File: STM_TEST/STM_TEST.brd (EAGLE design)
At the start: 59.9 x 69.6 mm, 53 parts, among them U1 TPS2115APWR, U2 AZ1117EH-3.3TRG1, Y1 ECS-80-S-4X, Y2 ECS-80-S-4X

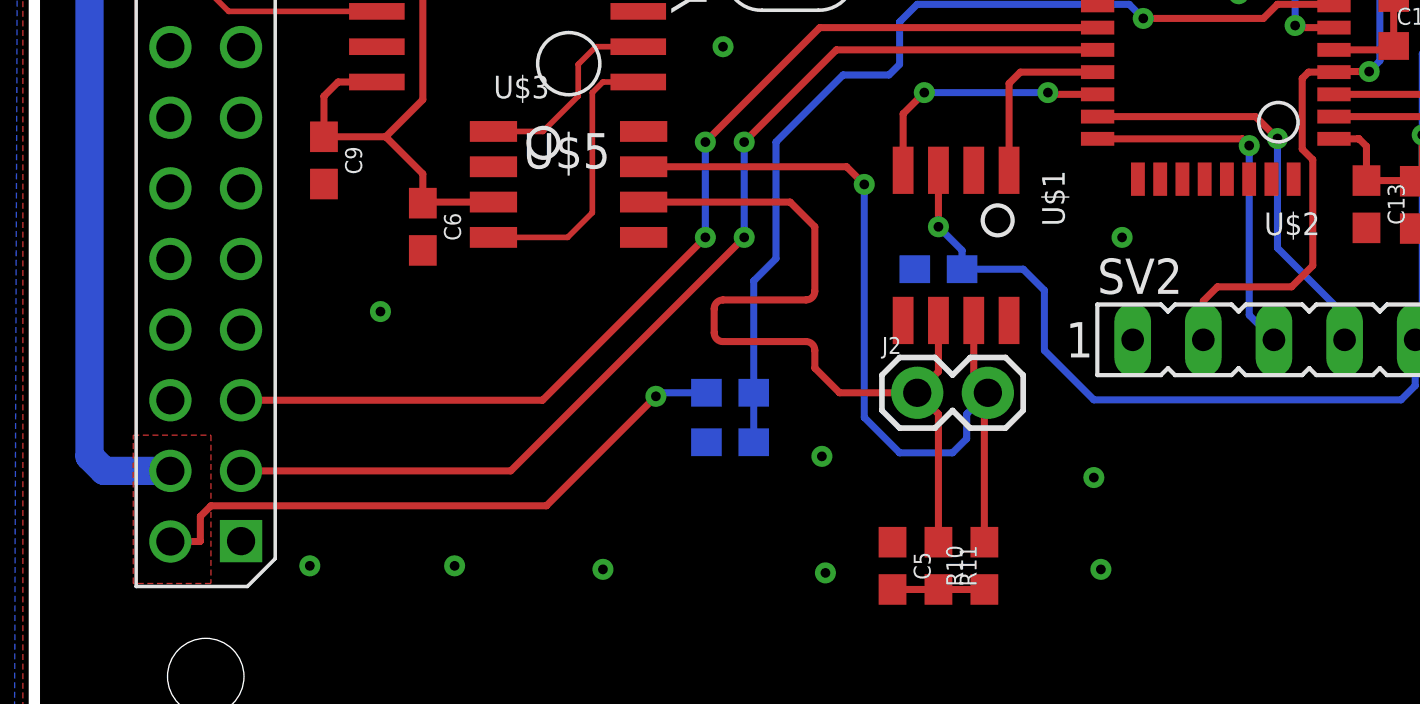
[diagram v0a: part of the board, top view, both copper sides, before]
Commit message: Routed USART
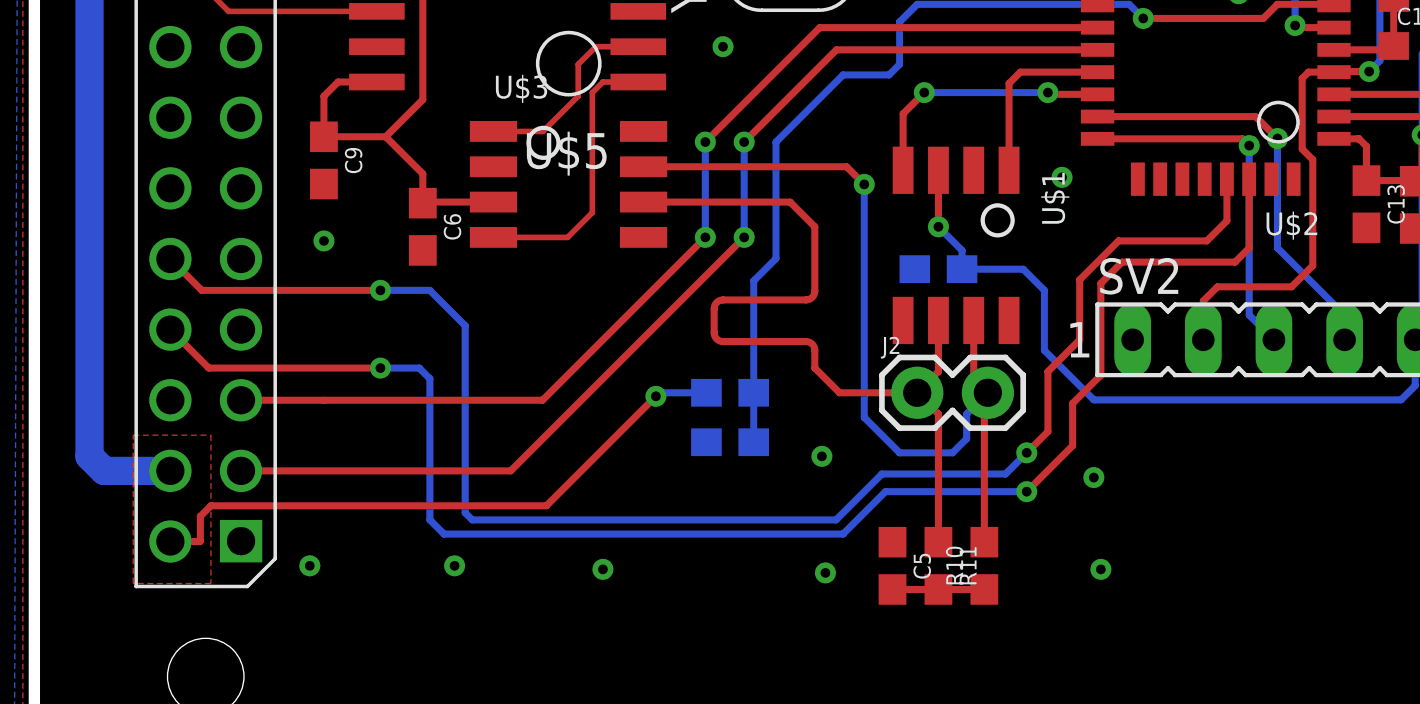
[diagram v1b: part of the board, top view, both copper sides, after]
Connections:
- removed net UART_RXD: PCB1.P$10
- removed net UART_TXD: PCB1.P$8
- new net USART_RX: PCB1.P$8, U$2.PB7
- new net USART_TX: PCB1.P$10, U$2.PB6
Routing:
- net USART_RX: track 0.00 -> 54.4 mm, vias 0 -> 2
- net USART_TX: track 0.00 -> 54.3 mm, vias 0 -> 2
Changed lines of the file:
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@@
 <via x="35.179" y="39.243" extent="1-16" drill="0.35"/>
 <via x="33.782" y="35.306" extent="1-16" drill="0.35"/>
-<via x="12.827" y="17.399" extent="1-16" drill="0.35"/>
+<via x="10.795" y="19.939" extent="1-16" drill="0.35"/>
 <via x="10.287" y="8.255" extent="1-16" drill="0.35"/>
 <via x="15.494" y="8.255" extent="1-16" drill="0.35"/>
@@
 <via x="56.642" y="13.335" extent="1-16" drill="0.35"/>
 <via x="57.023" y="9.398" extent="1-16" drill="0.35"/>
-<via x="39.497" y="20.066" extent="1-16" drill="0.35"/>
+<via x="37.338" y="22.225" extent="1-16" drill="0.35"/>
 <via x="25.146" y="26.924" extent="1-16" drill="0.35"/>
 <via x="40.259" y="59.055" extent="1-16" drill="0.35"/>
@@
 <wire x1="7.366" y1="28.194" x2="12.698" y2="28.194" width="0.2032" layer="1"/>
 </signal>
-<signal name="UART_RXD">
-<contactref element="PCB1" pad="P$10"/>
-</signal>
-<signal name="UART_TXD">
-<contactref element="PCB1" pad="P$8"/>
-</signal>
 <signal name="MISO">
 <contactref element="U$2" pad="PA6"/>
@@
 <contactref element="U$2" pad="PA9"/>
 <contactref element="PCB1" pad="P$5"/>
-<wire x1="7.8122" y1="14.2096" x2="18.6546" y2="14.2096" width="0.254" layer="1"/>
+<wire x1="7.8122" y1="14.2096" x2="10.795" y2="14.2096" width="0.254" layer="1"/>
+<wire x1="10.795" y1="14.2096" x2="18.6546" y2="14.2096" width="0.254" layer="1"/>
 <wire x1="18.6546" y1="14.2096" x2="24.511" y2="20.066" width="0.254" layer="1"/>
 <via x="24.511" y="20.066" extent="1-16" drill="0.35"/>
@@
 <wire x1="21.4" y1="67.608" x2="21.4" y2="65.087" width="1.016" layer="16"/>
 </signal>
+<signal name="USART_RX">
+<contactref element="U$2" pad="PB7"/>
+<contactref element="PCB1" pad="P$8"/>
+<wire x1="5.2722" y1="16.7496" x2="6.6548" y2="15.367" width="0.254" layer="1"/>
+<wire x1="6.6548" y1="15.367" x2="12.827" y2="15.367" width="0.254" layer="1"/>
+<via x="12.827" y="15.367" extent="1-16" drill="0.35"/>
+<wire x1="12.827" y1="15.367" x2="14.224" y2="15.367" width="0.254" layer="16"/>
+<wire x1="14.224" y1="15.367" x2="14.605" y2="14.986" width="0.254" layer="16"/>
+<wire x1="14.605" y1="14.986" x2="14.605" y2="9.906" width="0.254" layer="16"/>
+<wire x1="14.605" y1="9.906" x2="15.113" y2="9.398" width="0.254" layer="16"/>
+<wire x1="15.113" y1="9.398" x2="29.464" y2="9.398" width="0.254" layer="16"/>
+<wire x1="29.464" y1="9.398" x2="30.988" y2="10.922" width="0.254" layer="16"/>
+<via x="36.068" y="10.922" extent="1-16" drill="0.35"/>
+<wire x1="36.068" y1="10.922" x2="37.719" y2="12.573" width="0.254" layer="1"/>
+<wire x1="37.719" y1="12.573" x2="37.719" y2="14.097" width="0.254" layer="1"/>
+<wire x1="37.719" y1="14.097" x2="38.735" y2="15.113" width="0.254" layer="1"/>
+<wire x1="38.735" y1="15.113" x2="38.735" y2="18.415" width="0.254" layer="1"/>
+<wire x1="43.561" y1="19.177" x2="44.069" y2="19.685" width="0.254" layer="1"/>
+<wire x1="44.069" y1="19.685" x2="44.067" y2="19.687" width="0.254" layer="1"/>
+<wire x1="44.067" y1="19.687" x2="44.067" y2="22.16" width="0.254" layer="1"/>
+<wire x1="30.988" y1="10.922" x2="36.068" y2="10.922" width="0.254" layer="16"/>
+<wire x1="38.735" y1="18.415" x2="39.497" y2="19.177" width="0.254" layer="1"/>
+<wire x1="39.497" y1="19.177" x2="43.561" y2="19.177" width="0.254" layer="1"/>
+</signal>
+<signal name="USART_TX">
+<contactref element="U$2" pad="PB6"/>
+<contactref element="PCB1" pad="P$10"/>
+<wire x1="5.2722" y1="19.2896" x2="6.4008" y2="18.161" width="0.254" layer="1"/>
+<wire x1="6.4008" y1="18.161" x2="12.827" y2="18.161" width="0.254" layer="1"/>
+<via x="12.827" y="18.161" extent="1-16" drill="0.35"/>
+<wire x1="12.827" y1="18.161" x2="14.605" y2="18.161" width="0.254" layer="16"/>
+<wire x1="14.605" y1="18.161" x2="15.875" y2="16.891" width="0.254" layer="16"/>
+<wire x1="15.875" y1="16.891" x2="15.875" y2="10.16" width="0.254" layer="16"/>
+<wire x1="15.875" y1="10.16" x2="16.129" y2="9.906" width="0.254" layer="16"/>
+<wire x1="16.129" y1="9.906" x2="29.21" y2="9.906" width="0.254" layer="16"/>
+<wire x1="29.21" y1="9.906" x2="30.861" y2="11.557" width="0.254" layer="16"/>
+<wire x1="35.306" y1="11.557" x2="36.068" y2="12.319" width="0.254" layer="16"/>
+<via x="36.068" y="12.319" extent="1-16" drill="0.35"/>
+<wire x1="36.068" y1="12.319" x2="36.83" y2="13.081" width="0.254" layer="1"/>
+<wire x1="36.83" y1="15.24" x2="37.973" y2="16.383" width="0.254" layer="1"/>
+<wire x1="37.973" y1="18.542" x2="39.37" y2="19.939" width="0.254" layer="1"/>
+<wire x1="39.37" y1="19.939" x2="42.545" y2="19.939" width="0.254" layer="1"/>
+<wire x1="42.545" y1="19.939" x2="43.267" y2="20.661" width="0.254" layer="1"/>
+<wire x1="43.267" y1="20.661" x2="43.267" y2="22.16" width="0.254" layer="1"/>
+<wire x1="30.861" y1="11.557" x2="35.306" y2="11.557" width="0.254" layer="16"/>
+<wire x1="36.83" y1="13.081" x2="36.83" y2="15.24" width="0.254" layer="1"/>
+<wire x1="37.973" y1="16.383" x2="37.973" y2="18.542" width="0.254" layer="1"/>
+</signal>
 </signals>

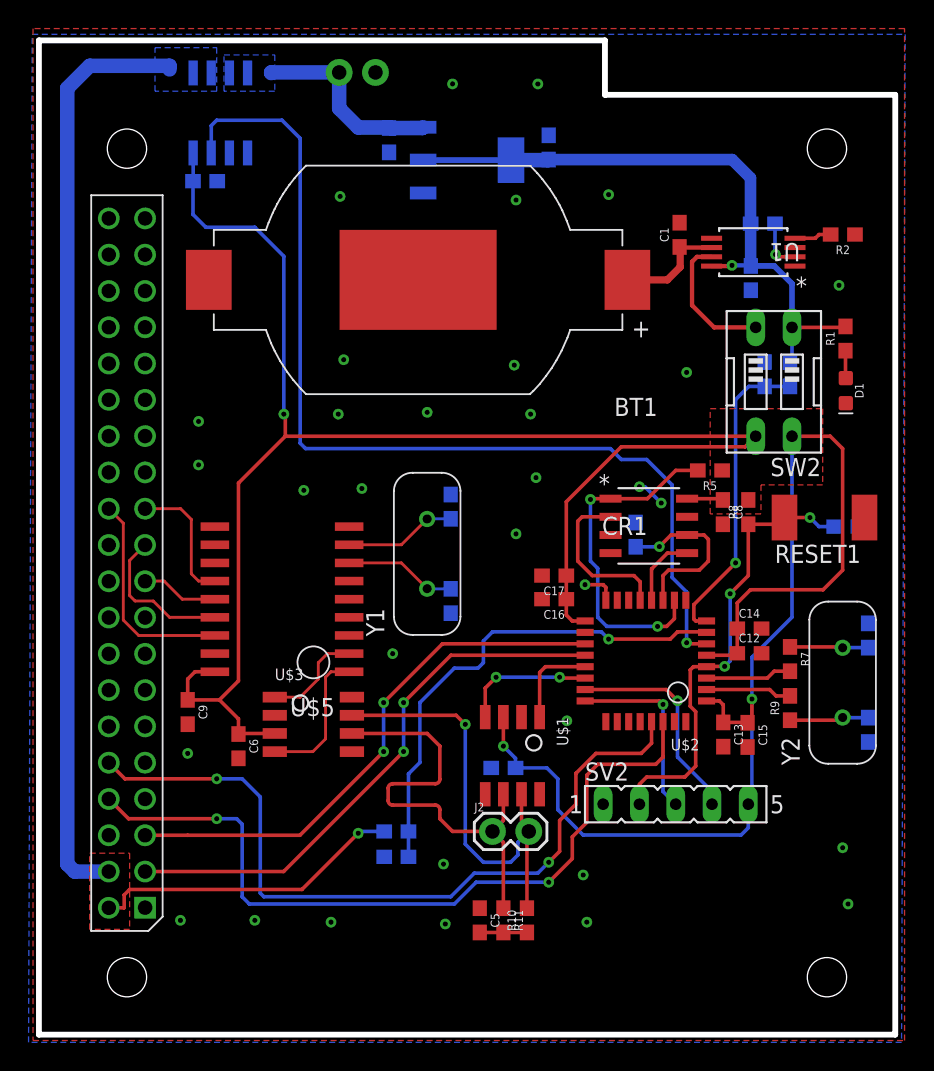
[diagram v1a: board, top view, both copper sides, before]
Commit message: Routing Complete
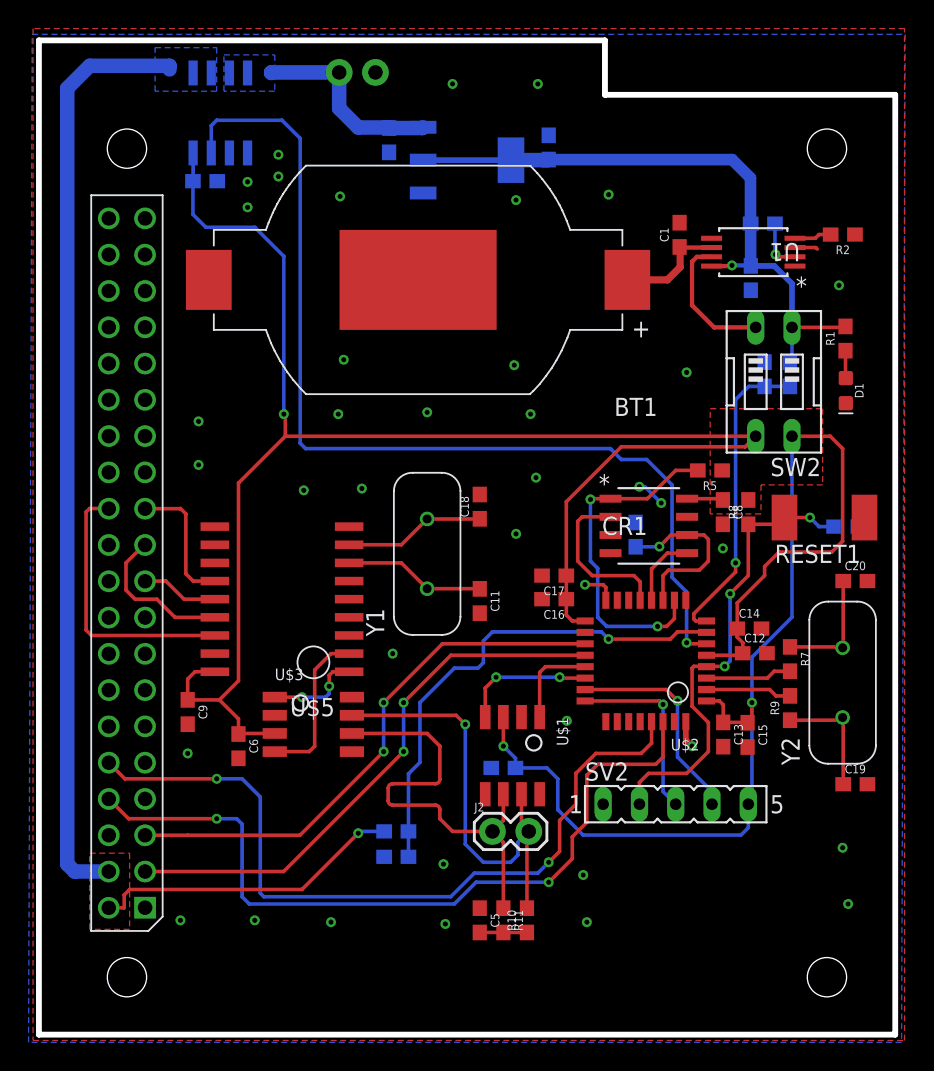
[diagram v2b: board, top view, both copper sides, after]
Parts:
- moved C19 3.91 mm to (57.5, 17.8), flipped to the top, turned to 0 degrees
- moved C20 3.91 mm to (57.5, 32.0), flipped to the top, turned to 0 degrees
- moved C11 2.03 mm to (31.2, 30.6), flipped to the top
- moved C18 2.03 mm to (31.2, 37.2), flipped to the top
- moved C12 0.38 mm to (50.5, 26.9)
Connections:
- net CAN_PI_RX: now also U$3.RXD; no longer U$3.TXD
- net CAN_PI_TX: now also U$3.TXD; no longer U$3.RXD
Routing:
- net CE0: track 15.1 -> 19.1 mm
- net CAN_PI_RX: track 7.14 -> 11.2 mm
- net GND: track 4.44 -> 7.93 mm, vias 33 -> 39
- net CAN_PI_TX: track 10.1 -> 6.69 mm, vias 0 -> 2
- net N$7: track 5.56 -> 8.45 mm
- net N$6: track 5.51 -> 8.40 mm
- net OSC2: track 7.88 -> 9.90 mm
- net OSC1: track 7.88 -> 9.90 mm
- net NRST: track 32.4 -> 33.0 mm
- net +3V3: track 201.1 -> 200.5 mm

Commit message: finished
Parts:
- added D2: (no value), SparkFun-LED:LED-0603
- added R15: 10k, SparkFun-Resistors:0603
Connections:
- new net N$4: D2.A, R15.1
- new net N$5: R15.2, U$2.PB4
- net GND: now also D2.C
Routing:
- net N$5: track 0.00 -> 9.44 mm, vias 0 -> 2
- net N$4: track 0.00 -> 2.34 mm
- net GND: track 7.93 -> 9.81 mm
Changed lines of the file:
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@@
 <wire x1="60.325" y1="0.254" x2="0.381" y2="0.254" width="0.4064" layer="20"/>
 <wire x1="0.381" y1="0.254" x2="0.381" y2="69.85" width="0.4064" layer="20"/>
-<text x="42.291" y="4.699" size="1.016" layer="48">Data_Logger_rev1
+<text x="42.291" y="4.699" size="1.016" layer="21">Data_Logger_rev1
 Designed By:
 Jacob Bobson
@@
 <attribute name="PROD_ID" value="CAP-00868" x="45.974" y="46.355" size="1.778" layer="28" rot="MR90" display="off"/>
 </element>
+<element name="R15" library="SparkFun-Resistors" library_urn="urn:adsk.eagle:library:532" package="0603" package3d_urn="urn:adsk.eagle:package:39650/1" value="10k" x="40.894" y="12.192" rot="R90">
+<attribute name="PROD_ID" value="RES-07828" x="37.465" y="12.192" size="1.778" layer="27" rot="R90" display="off"/>
+</element>
+<element name="D2" library="SparkFun-LED" package="LED-0603" value="" x="40.894" y="8.128" rot="R270"/>
 </elements>
 <signals>
@@
 <via x="17.145" y="61.849" extent="1-16" drill="0.35"/>
 <via x="14.986" y="58.166" extent="1-16" drill="0.35"/>
-<wire x1="50.9642" y1="28.6766" x2="51.3452" y2="26.9494" width="0" layer="19" extent="1-1"/>
+<contactref element="D2" pad="C"/>
+<wire x1="50.9642" y1="28.6766" x2="50.9642" y2="28.0298" width="0.3048" layer="1"/>
+<wire x1="51.3452" y1="27.6488" x2="51.3452" y2="26.9494" width="0.3048" layer="1"/>
+<wire x1="50.9642" y1="28.0298" x2="51.3452" y2="27.6488" width="0.3048" layer="1"/>
 </signal>
 <signal name="+3V3BAT">
@@
 <wire x1="37.973" y1="16.383" x2="37.973" y2="18.542" width="0.254" layer="1"/>
 </signal>
+<signal name="N$4">
+<contactref element="R15" pad="1"/>
+<contactref element="D2" pad="A"/>
+<wire x1="40.894" y1="9.005" x2="40.894" y2="11.342" width="0.3048" layer="1"/>
+</signal>
+<signal name="N$5">
+<contactref element="U$2" pad="PB4"/>
+<contactref element="R15" pad="2"/>
+<wire x1="40.894" y1="13.042" x2="40.894" y2="14.986" width="0.3048" layer="1"/>
+<wire x1="40.894" y1="14.986" x2="41.148" y2="15.24" width="0.3048" layer="1"/>
+<wire x1="41.148" y1="15.24" x2="41.148" y2="17.907" width="0.3048" layer="1"/>
+<via x="41.148" y="17.907" extent="1-16" drill="0.35"/>
+<wire x1="41.148" y1="17.907" x2="41.148" y2="20.193" width="0.3048" layer="16"/>
+<wire x1="41.148" y1="20.193" x2="41.656" y2="20.701" width="0.3048" layer="16" curve="-90"/>
+<via x="41.656" y="20.701" extent="1-16" drill="0.35"/>
+<wire x1="41.656" y1="20.701" x2="41.656" y2="22.149" width="0.3048" layer="1"/>
+<wire x1="41.656" y1="22.149" x2="41.667" y2="22.16" width="0.3048" layer="1" curve="-90"/>
+</signal>
 </signals>
